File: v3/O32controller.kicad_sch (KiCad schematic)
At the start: 43 parts, among them J1 SWD, J10 3V3, J11 GND, J12 I2C/RS485_2, J2 BATT+, J3 BATT-, J7 BATT+, J8 BATT-, J9 I2C/RS485_1, SW1 RESET, U1 MA702GQ-P, U2 STSPIN32F0A, U3 THVD1420DRLR

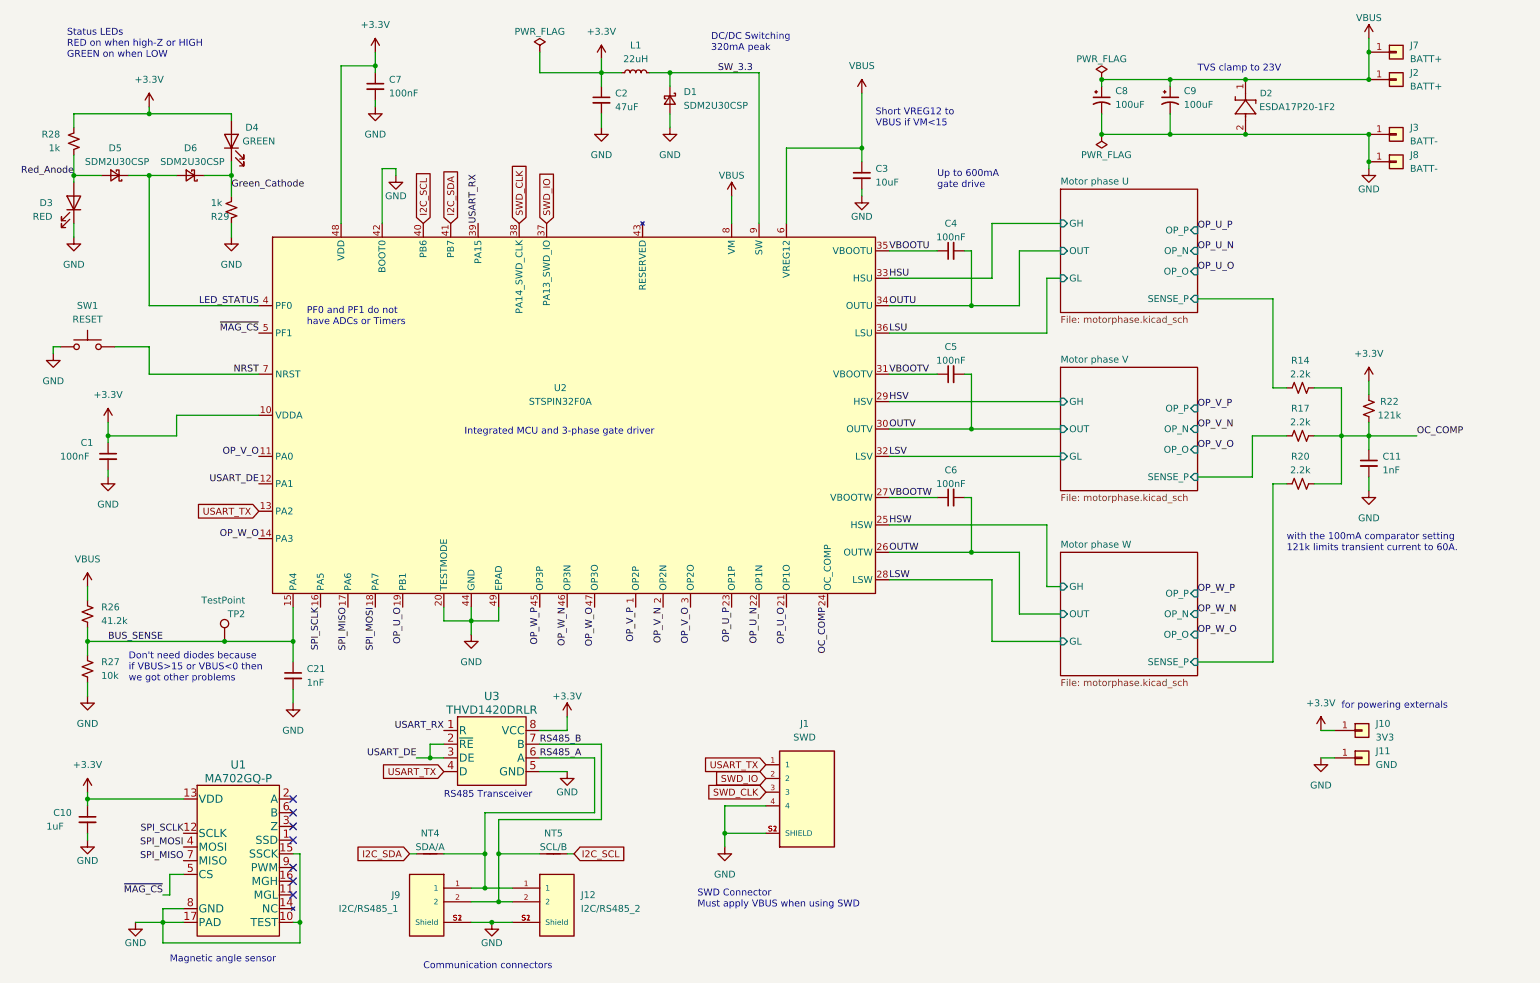
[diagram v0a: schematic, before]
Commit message: external spi, update bus sns res, routing
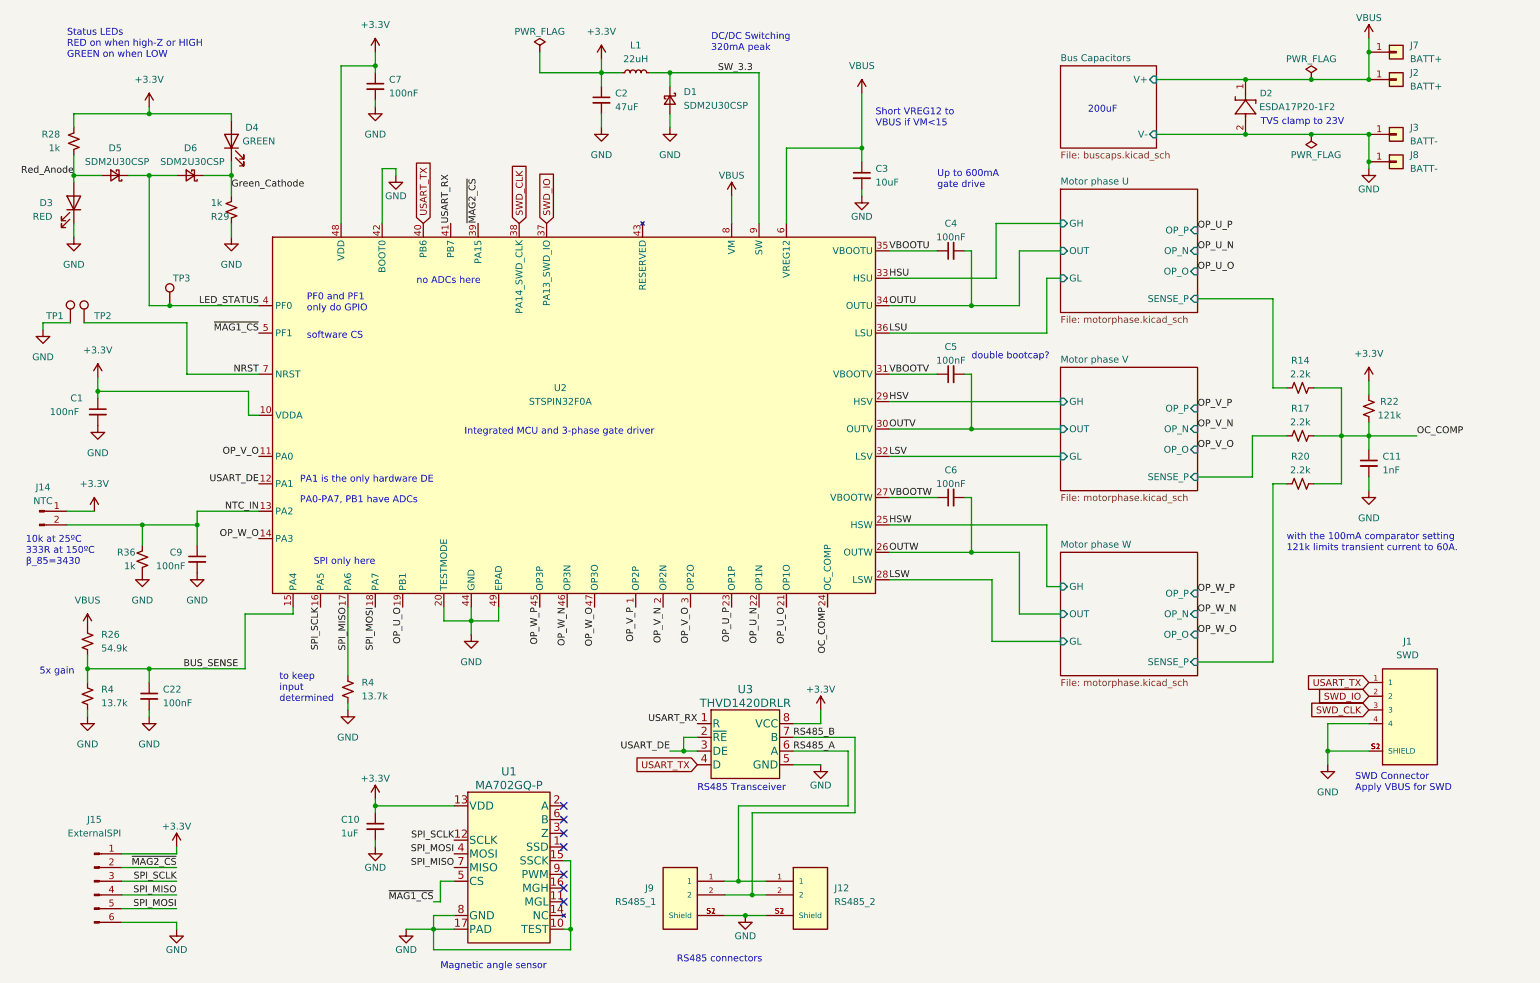
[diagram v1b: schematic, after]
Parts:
- removed C21: 1nF, Capacitor_SMD:C_0402_1005Metric, symbol Device:C_Small
- removed C8, C9: 100uF, O32controller:CAP_EEEFN1E101UP, symbol Device:C_Polarized_Small_US
- removed J10: 3V3, O32controller:SolderWire-Actual_1x01_D1.25mm_OD_1.8mm, symbol Connector_Generic:Conn_01x01
- removed J11: GND, O32controller:SolderWire-Actual_1x01_D1.25mm_OD_1.8mm, symbol Connector_Generic:Conn_01x01
- removed NT4: SDA/A, O32controller:NetTie-2_SMD_Pad0.25mm, symbol Device:NetTie_2
- removed NT5: SCL/B, O32controller:NetTie-2_SMD_Pad0.25mm, symbol Device:NetTie_2
- removed R27: 10k, Resistor_SMD:R_0402_1005Metric, symbol Device:R_Small_US
- removed SW1: RESET, O32controller:Tactile_Switch_EVQ-P7A01P, symbol Switch:SW_Push
- added C22, C9: 100nF, Capacitor_SMD:C_0402_1005Metric, symbol Device:C_Small
- added J14: NTC, O32controller:SolderNTC-1.27mm, symbol Connector:Conn_01x02_Pin
- added J15: ExternalSPI, O32controller:FFC_0.5mm_6p, symbol Connector:Conn_01x06_Pin
- added R36: 1k, Resistor_SMD:R_0402_1005Metric, symbol Device:R_Small_US
- added R4 (x2): 13.7k, Resistor_SMD:R_0402_1005Metric, symbol Device:R_Small_US
- added TP1, TP2: TestPoint, TestPoint:TestPoint_Pad_D1.0mm, symbol Connector:TestPoint
- J12: value I2C/RS485_2 -> RS485_2
- J9: value I2C/RS485_1 -> RS485_1
- R26: value 41.2k -> 54.9k; MP RC0402FR-0741K2L -> RC0402FR-0754K9L
- renumbered TP2 to TP3
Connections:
- net I2C_SCL is gone; now on net USART_TX: U2.40 (PB6)
- net I2C_SDA is gone; now on net USART_RX: U2.41 (PB7)
- net +3.3V: now also J14.1 (Pin_1), J15.1 (Pin_1)
- net BUS_SENSE: now also C22.1, R4.2; no longer TP3.1
- net GND: now also C22.2, C9.2, J15.6 (Pin_6), R36.1, R4.1, R4.1, TP1.1
- net LED_STATUS: now also TP3.1
- net NRST: now also TP2.1
- net SPI_MISO: now also J15.4 (Pin_4), R4.2
- net SPI_MOSI: now also J15.5 (Pin_5)
- net SPI_SCLK: now also J15.3 (Pin_3)
- net USART_RX: no longer U2.39 (PA15)
- net USART_TX: no longer U2.13 (PA2)
- net ~{MAG_CS} renamed ~{MAG1_CS}
- new net NTC_IN: C9.1, J14.2 (Pin_2), R36.2, U2.13 (PA2)
- new net ~{MAG2_CS}: J15.2 (Pin_2), U2.39 (PA15)
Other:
- added sheet Bus Capacitors (buscaps.kicad_sch)
- note added: "10k at 25ºC 333R at 150ºC β_85=3430"
- note added: "200uF"
- note added: "5x gain"
- note added: "PA0-PA7, PB1 have ADCs"
- note added: "PA1 is the only hardware DE"
- note added: "PF0 and PF1 only do GPIO"
- note added: "RS485 connectors"
- note added: "SPI only here"
- note added: "SWD Connector Apply VBUS for SWD"
- note added: "double bootcap?"
- note added: "no ADCs here"
- note added: "software CS"
- note added: "to keep input determined"
- note removed: "Communication connectors"
- note removed: "Don't need diodes because if VBUS>15 or VBUS<0 then we got other problems"
- note removed: "PF0 and PF1 do not have ADCs or Timers"
- note removed: "SWD Connector Must apply VBUS when using SWD"
- note removed: "for powering externals"
- company: (none) -> Christopher Xu
- moved on the sheet: C1, C10, J1, J12, J9, R26, TP3, U1, U3

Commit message: bus caps, finished routing?
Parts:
- removed TP1: TestPoint, TestPoint:TestPoint_Pad_D1.0mm, symbol Connector:TestPoint
- TP1: renamed from TP3; footprint TestPoint:TestPoint_Pad_D1.0mm -> O32controller:TestPoint_Pad_Rect
- TP3: renamed from TP2; footprint TestPoint:TestPoint_Pad_D1.0mm -> O32controller:TestPoint_Pad_Rect
- renumbered C7 to C1, C22 to C10, C10 to C11, C1 to C6, C11 to C7, C6 to C8, D4 to D3, D5 to D4, D6 to D5, D3 to D6, J7 to J1, J8 to J4, J14 to J5, J1 to J6, J15 to J7, J9 to J8, J12 to J9, R28 to R1, R29 to R2, R14 to R3, R22 to R4, R17 to R5, R20 to R6, R36 to R7, R26 to R8, U2 to U1, U3 to U2, U1 to U3
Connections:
- net +3.3V: now also J7.6 (Pin_6); no longer J7.1 (Pin_1)
- net GND: now also J7.1 (Pin_1); no longer J7.6 (Pin_6)
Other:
- note added: "36x 22uF 25V 0805 103uF at 15V"
- note added: "short to GND to reset"
- note removed: "200uF"
- moved on the sheet: TP3

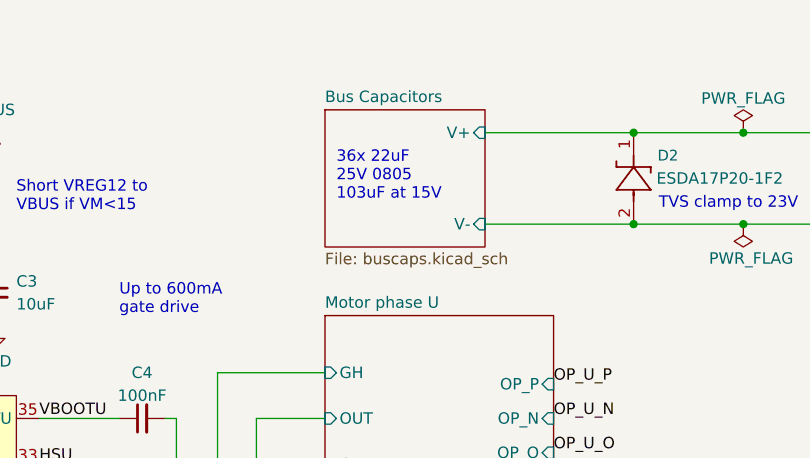
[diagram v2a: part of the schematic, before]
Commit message: import pcbway cheapest capability drc rules
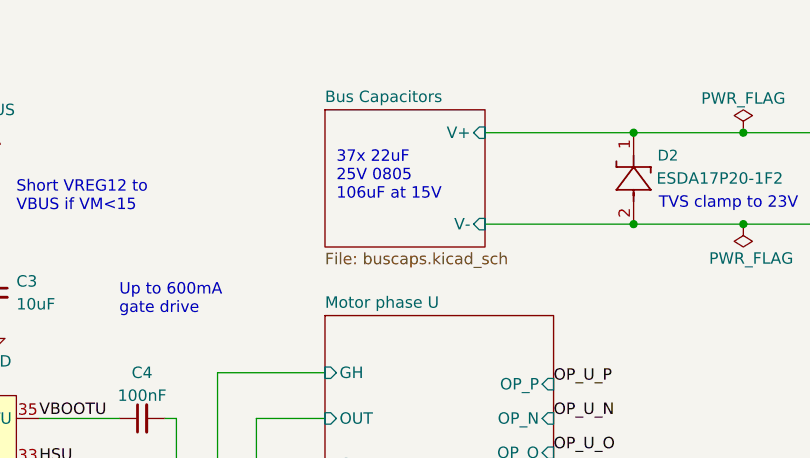
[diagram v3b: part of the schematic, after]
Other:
- note added: "37x 22uF 25V 0805 106uF at 15V"
- note removed: "36x 22uF 25V 0805 103uF at 15V"
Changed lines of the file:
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@@
     (effects (font (size 1.27 1.27)) (justify left bottom))
   )
-  (text "36x 22uF\n25V 0805\n103uF at 15V" (at 207.01 35.56 0)
+  (text "37x 22uF\n25V 0805\n106uF at 15V" (at 207.01 35.56 0)
     (effects (font (size 1.27 1.27)) (justify left bottom))
   )

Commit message: export for PCBway
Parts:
- added C58: 100nF, Capacitor_SMD:C_0402_1005Metric, symbol Device:C_Small
- C1, C10, C4, C5, C6, C8, C9: MP CL05A104KA5NNNC -> (none); MPN (none) -> CL05A104KA5NNNC; Vendor (none) -> LCSC; Vendor# (none) -> C100072
- C11: MP GCM155C71A105KE38D -> (none); MPN (none) -> GCM155C71A105KE38D; Vendor (none) -> LCSC; Vendor# (none) -> C126521
- C2: MP GRM188R60J476ME15D -> (none); MPN (none) -> GRM188R60J476ME15D; Vendor (none) -> LCSC; Vendor# (none) -> C140782
- C3: MP GRM188R6YA106MA73D -> (none); MPN (none) -> GRM188R6YA106MA73D; Vendor (none) -> LCSC; Vendor# (none) -> C194427
- C7: MP CC0402MRX7R9BB102 -> (none); MPN (none) -> CC0402MRX7R9BB102; Vendor (none) -> LCSC; Vendor# (none) -> C527029
- D1, D4, D5: MP SDM2U30CSP -> (none); MPN (none) -> SDM2U30CSP-7; Vendor (none) -> LCSC; Vendor# (none) -> C3001723
- D2: MP ESDA17P20-1F2 -> (none); MPN (none) -> ESDA17P20-1F2; Vendor (none) -> LCSC; Vendor# (none) -> C3713569
- D3: MP 150060VS55040 -> (none); MPN (none) -> LTST-C191KGKT; Vendor (none) -> LCSC; Vendor# (none) -> C125098
- D6: MP 150060RS55040 -> (none); MPN (none) -> LTST-C191KRKT; Vendor (none) -> LCSC; Vendor# (none) -> C125099
- J6: MP SM04B-SRSS-TB(LF)(SN) -> (none); MPN (none) -> SM04B-SRSS-TB(LF)(SN); Vendor (none) -> LCSC; Vendor# (none) -> C160404
- J8: value RS485_1 -> RS485; MP SM02B-SRSS-TB_LF__SN_ -> (none); MPN (none) -> SM02B-SRSS-TB_LF__SN_; Vendor (none) -> LCSC; Vendor# (none) -> C160402
- J9: value RS485_2 -> RS485; MP SM02B-SRSS-TB_LF__SN_ -> (none); MPN (none) -> SM02B-SRSS-TB_LF__SN_; Vendor (none) -> LCSC; Vendor# (none) -> C160402
- L1: MP VLS201612CX-220M-1 -> (none); MPN (none) -> VLS201612CX-220M-1; Vendor (none) -> LCSC; Vendor# (none) -> C2044426
- R1, R2: MP RC0402FR-071KL -> (none); MPN (none) -> RC0402FR-071KL; Vendor (none) -> LCSC; Vendor# (none) -> C106235
- R3, R5, R6: MP RC0402FR-072K2L -> (none); MPN (none) -> RC0402FR-072K2L; Vendor (none) -> LCSC; Vendor# (none) -> C114762
- R4: MP RC0402FR-07121KL -> (none); MPN (none) -> AF0402FR-07121KL; Vendor (none) -> LCSC; Vendor# (none) -> C4153138
- R4: MP RC0402FR-0713K7L -> (none); MPN (none) -> RC0402FR-0713K7L; Vendor (none) -> LCSC; Vendor# (none) -> C274888
- R7: MPN (none) -> RC0402FR-071KL; Vendor (none) -> LCSC; Vendor# (none) -> C106235
- R8: MP RC0402FR-0754K9L -> (none); MPN (none) -> RC0402FR-0754K9L; Vendor (none) -> LCSC; Vendor# (none) -> C137959
- U1: value STSPIN32F0A -> STSPIN32F0ATR; MP STSPIN32F0A -> (none); MPN (none) -> STSPIN32F0ATR; Vendor (none) -> LCSC; Vendor# (none) -> C2651733
- U2: MP THVD1420DRLR -> (none); MPN (none) -> THVD1420DRLR; Vendor (none) -> Digikey; Vendor# (none) -> 296-THVD1420DRLRCT-ND
- U3: MP MA702GQ-P -> (none); MPN (none) -> MA702GQ-P; Vendor (none) -> MPS; Vendor# (none) -> MA702GQ
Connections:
- net GND: now also C58.2
- net NRST: now also C58.1
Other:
- note added: "Status LEDs RED on when HIGH GREEN on when LOW Both on when high-Z"
- note removed: "Status LEDs RED on when high-Z or HIGH GREEN on when LOW"
- note removed: "double bootcap?"
- moved on the sheet: C6

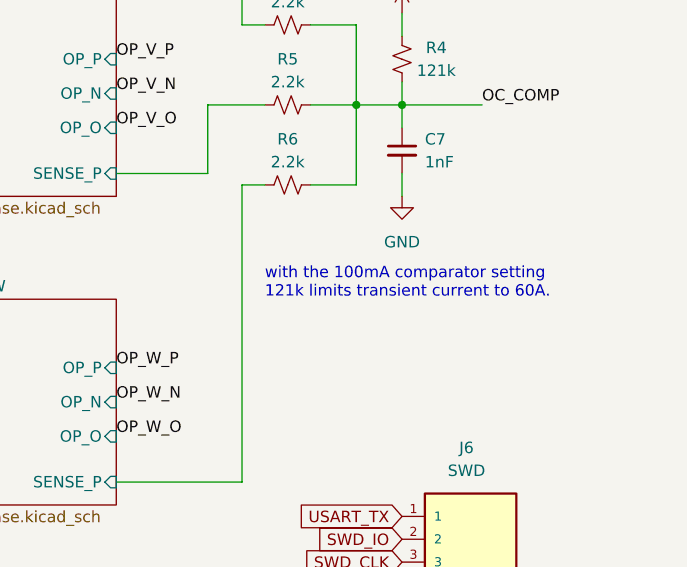
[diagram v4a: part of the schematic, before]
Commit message: fixed note with OC comparator, 60A 121k error
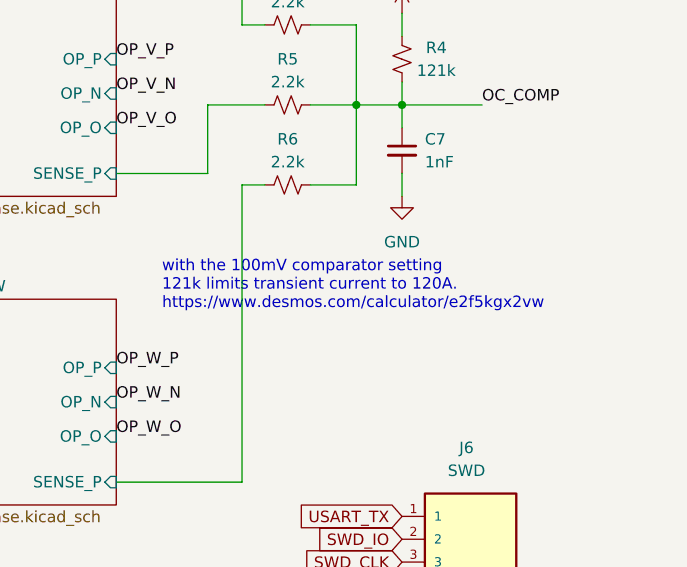
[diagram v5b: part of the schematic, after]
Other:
- note added: "with the 100mV comparator setting 121k limits transient current to 120A. https://www.desmos.com/calculator/e2f5kgx2vw"
- note removed: "with the 100mA comparator setting 121k limits transient current to 60A."
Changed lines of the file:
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@@
     (effects (font (size 1.27 1.27)) (justify left bottom))
   )
-  (text "with the 100mA comparator setting\n121k limits transient current to 60A."
-    (at 247.65 115.57 0)
+  (text "with the 100mV comparator setting\n121k limits transient current to 120A.\nhttps://www.desmos.com/calculator/e2f5kgx2vw"
+    (at 236.22 116.84 0)
     (effects (font (size 1.27 1.27)) (justify left bottom))
   )
